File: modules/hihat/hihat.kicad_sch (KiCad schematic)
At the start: 26 parts, among them U1 VTL5C, U2 MCP6002-xSN

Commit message: Implement the gate to pulse generator.
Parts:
- added C3: 10nf, symbol Device:C
- added C6, C7: 0.1uf, Capacitor_SMD:C_0402_1005Metric, symbol Device:C
- added D1: SS8050, Package_TO_SOT_SMD:SOT-23, symbol Power_Protection:ESDA5V3L
- added R12, R15, R16: 100k, symbol Device:R
- added R13: 330, symbol Device:R
- added R14: 10k, symbol Device:R
- added R17, R18: 1M, symbol Device:R
- added U3, U4: MCP6002-xSN, Package_SO:SOIC-8-1EP_3.9x4.9mm_P1.27mm_EP2.29x3mm, symbol Amplifier_Operational:MCP6002-xSN
- added V4: VPULSE, symbol Simulation_SPICE:VPULSE
- added V5: VSIN, symbol Simulation_SPICE:VSIN
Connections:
- net GND: now also C6.1, C7.1, R12.1, R16.1, U3.4 (V-), U4.4 (V-), V4.2, V5.2
- net V_MID: now also U3.2 (-)
- net V_SUPPLY: now also C6.2, C7.2, R14.2, R18.2, U3.8 (V+), U4.8 (V+)
- new net: C3.2, R12.2, U3.3 (+)
- new net: R17.2, R18.1, U3.5 (+)
- new net: D1.3 (A), U3.6 (-), U3.7
- new net: D1.1 (K), R13.2
- new net: R15.1, R16.2, R17.1
- new net: R13.1, U3.1
- new net CV_ACCENT: R14.1, R15.2, V5.1
- new net GATE_IN: C3.1, V4.1
- new net PULSE_OUT: D1.2 (K)
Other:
- note added: "## GATE TO PULSE GENERATOR Generate a short pulse based on a given gate. We also have some accent control too."
- note added: "## Vactrols based VCA Here we don't need to voltage to current conversion setup. We just need to map the TRANSIENT_CV input to 1.65v to 3.3v."
- moved on the sheet: C1, U2C

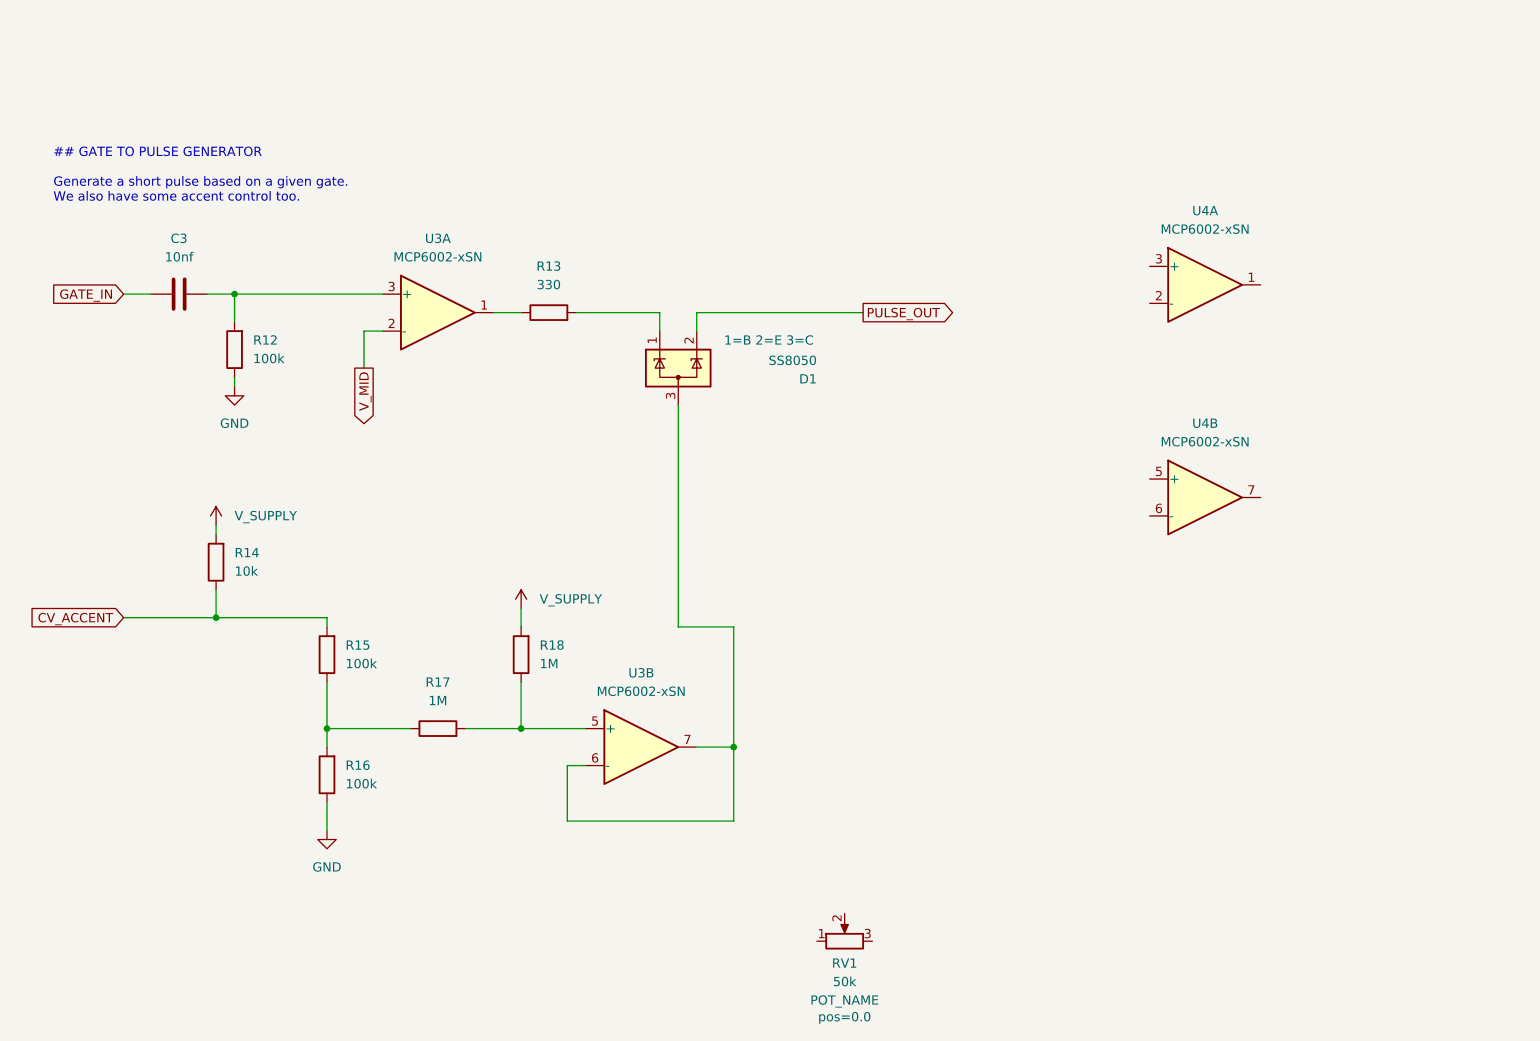
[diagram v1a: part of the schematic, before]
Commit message: Add a opamp buffer for the CV_ACCENT
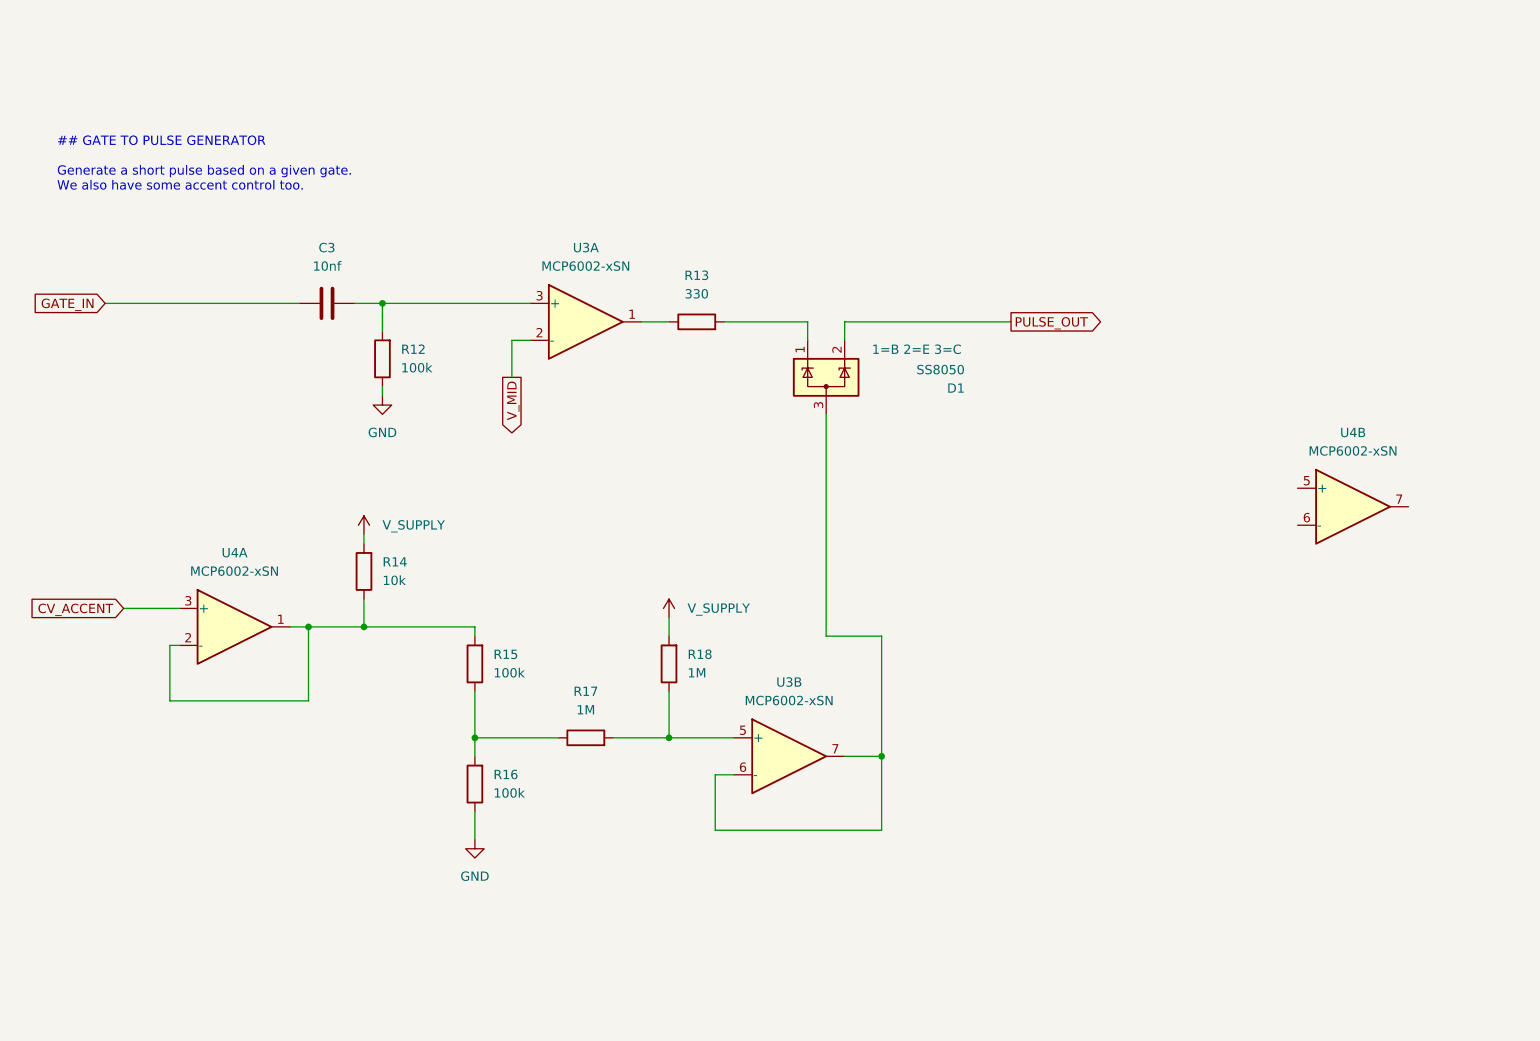
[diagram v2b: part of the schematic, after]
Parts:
- removed RV1: 50k, BreadModular_Pots:Potentiometer_RV09, symbol Device:R_Potentiometer
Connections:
- net CV_ACCENT: now also U4.3 (+); no longer R14.1, R15.2
- net at U4.1: now also R14.1, R15.2, U4.2 (-)
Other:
- moved on the sheet: C3, D1, R12, R13, R14, R15, R16, R17, R18, U3A, U3B, U4A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

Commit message: Finished schematics
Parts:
- added C8: 4.7uf, Capacitor_SMD:C_0603_1608Metric, symbol Device:C
- added D2: SS14, Diode_SMD:D_SMA, symbol Diode:SS210
- added D3: SS8050, Package_TO_SOT_SMD:SOT-23, symbol Power_Protection:ESDA5V3L
- added D4: SS8550, Package_TO_SOT_SMD:SOT-23, symbol Power_Protection:ESDA5V3L
- added R19: 22k, symbol Device:R
- added R20: 330, symbol Device:R
- added R21: 10k, symbol Device:R
- added R22, R23: 100k, symbol Device:R
- added R24: 200k, symbol Device:R
- added RV1: 50k, BreadModular_Pots:Potentiometer_RV09, symbol Device:R_Potentiometer
- R14: value 10k -> 100k
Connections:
- net CV_ACCENT: now also R14.1
- net GND: now also C8.1, D4.3 (A), R19.1, R21.1, R23.1, R24.1
- net PULSE_OUT: now also D2.2 (A)
- net TRANSIENT_CV: now also U4.7, R22.2; no longer V2.1
- net V_SUPPLY: now also D3.3 (A), D4.1 (K), R24.2
- net at R15.2, U4.1, U4.2 (-): no longer R14.1
- net at U4.5 (+): now also D3.2 (K), R21.2
- net at U4.6 (-): now also R22.1, R23.2
- new net: R20.1, RV1.1
- new net: D4.2 (K), RV1.2
- new net: C8.2, D2.1 (K), D3.1 (K), R19.2, R20.2
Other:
- note added: "## PULSE TO TRANSIENT GENERATOR Here we also allow a gate for Open HiHat as well."
- moved on the sheet: R14, U4A, U4B

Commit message: Started basic pcb layout
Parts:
- added R25: 1k, Resistor_SMD:R_0402_1005Metric, symbol Device:R
- C1: renamed from C2; footprint (none) -> Capacitor_SMD:C_0402_1005Metric
- C2: renamed from C4; footprint (none) -> Capacitor_SMD:C_0402_1005Metric
- C3: renamed from C5; footprint (none) -> Capacitor_SMD:C_0402_1005Metric
- C7: renamed from C3; footprint (none) -> Capacitor_SMD:C_0402_1005Metric
- R1: renamed from R6; footprint (none) -> Resistor_SMD:R_0402_1005Metric
- R10: renamed from R11; footprint (none) -> Resistor_SMD:R_0402_1005Metric
- R11: renamed from R5; footprint (none) -> Resistor_SMD:R_0402_1005Metric
- R12: renamed from R13; footprint (none) -> Resistor_SMD:R_0402_1005Metric
- R13: renamed from R12; footprint (none) -> Resistor_SMD:R_0402_1005Metric
- R14: renamed from R19; footprint (none) -> Resistor_SMD:R_0402_1005Metric
- R15: renamed from R20; footprint (none) -> Resistor_SMD:R_0402_1005Metric
- R16: renamed from R21; footprint (none) -> Resistor_SMD:R_0402_1005Metric
- R17: renamed from R22; footprint (none) -> Resistor_SMD:R_0402_1005Metric
- R18: renamed from R23; footprint (none) -> Resistor_SMD:R_0402_1005Metric
- R19: renamed from R14; value 100k -> 10k; footprint (none) -> Resistor_SMD:R_0402_1005Metric
- R2: renamed from R3; footprint (none) -> Resistor_SMD:R_0402_1005Metric
- R20: renamed from R24; footprint (none) -> Resistor_SMD:R_0402_1005Metric
- R21: renamed from R15; footprint (none) -> Resistor_SMD:R_0402_1005Metric
- R22: renamed from R18; footprint (none) -> Resistor_SMD:R_0402_1005Metric
- R23: renamed from R17; footprint (none) -> Resistor_SMD:R_0402_1005Metric
- R24: renamed from R16; footprint (none) -> Resistor_SMD:R_0402_1005Metric
- R3: renamed from R7; footprint (none) -> Resistor_SMD:R_0402_1005Metric
- R4: footprint (none) -> Resistor_SMD:R_0402_1005Metric
- R5: renamed from R8; footprint (none) -> Resistor_SMD:R_0402_1005Metric
- R6: renamed from R9; footprint (none) -> Resistor_SMD:R_0402_1005Metric
- R7: renamed from R1; footprint (none) -> Resistor_SMD:R_0402_1005Metric
- R8: renamed from R2; footprint (none) -> Resistor_SMD:R_0402_1005Metric
- R9: renamed from R10; footprint (none) -> Resistor_SMD:R_0402_1005Metric
- renumbered C6 to C4, C7 to C5, C1 to C6, D3 to D1, D1 to D3, RV2 to RV1, RV1 to RV2, V4 to V3, V3 to V4
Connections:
- net CV_ACCENT: now also INPUT1.3 (Pin_3), R21.2; no longer U4.3 (+)
- net GATE_IN: now also INPUT1.2 (Pin_2)
- net HIHAT_OUT: now also OUTPUT1.1 (Pin_1), OUTPUT1.2 (Pin_2), OUTPUT1.3 (Pin_3)
- net NOISE_IN: now also INPUT1.1 (Pin_1)
- net TRANSIENT_CV: now also U4.1, U4.5 (+); no longer U4.7
- net V_SUPPLY: no longer D4.1 (K), R20.2
- net at R17.1, R18.2: now also U4.2 (-); no longer U4.6 (-)
- net at D1.2 (K), R16.2: now also U4.3 (+); no longer U4.5 (+)
- net CV_OUT: now reaches OUTPUT1.4 (Pin_4)
- net CV_OUT: now also OUTPUT1.5 (Pin_5), R25.2
- net GATE_OPEN: now reaches INPUT1.4 (Pin_4)
- net GATE_OPEN: now also D4.1 (K), R20.2
- new net: R25.1, U4.6 (-), U4.7
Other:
- moved on the sheet: C4, C5, C6, U2C, U3C, U4C

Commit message: hihat: Add MIDI support Now we don't need seperate cables for GATE, Accent & Open Hat. We can control all these via a single MIDI cable.
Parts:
- added C9: 100uf, Capacitor_SMD:C_1206_3216Metric, symbol Device:C
- added R26: 4.7k, Resistor_SMD:R_0402_1005Metric, symbol Device:R
- added R27: 10k, Resistor_SMD:R_0402_1005Metric, symbol Device:R
- added U5: ATtiny1616-M, Package_DFN_QFN:VQFN-20-1EP_3x3mm_P0.4mm_EP1.7x1.7mm, symbol MCU_Microchip_ATtiny:ATtiny1616-M
- added V_SUPPLY2: Conn_01x05_Pin, BreadModular_MISC:Conn_Holes_2, symbol Connector:Conn_01x02_Pin
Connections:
- net CV_ACCENT: now also INPUT1.4 (Pin_4); no longer INPUT1.3 (Pin_3)
- net GATE_IN: now also INPUT1.3 (Pin_3), R27.1; no longer INPUT1.2 (Pin_2)
- net GATE_OPEN: now also INPUT1.5 (Pin_5); no longer INPUT1.4 (Pin_4)
- net GND: now also C9.1, U5.21 (GND), U5.3 (GND); no longer R20.1
- net V_SUPPLY: now also C9.2, U5.4 (VCC); no longer R19.2
- new net: R26.1, U5.19 (~{RESET}/PA0)
- new net MIDI: INPUT1.2 (Pin_2), U5.11 (PB3)
- new net MIDI_GATE: R27.2, U5.6 (PA5)
- new net MIDI_OPEN: R20.1, U5.8 (PA7)
- new net MIDI_VELOCITY: R19.2, U5.7 (PA6)
- new net TX: U5.12 (PB2), V_SUPPLY2.1 (Pin_1)
- new net UDPI: R26.2, V_SUPPLY2.2 (Pin_2)
